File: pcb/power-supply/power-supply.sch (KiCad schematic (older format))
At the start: 2 parts

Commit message: starting pcb design and added teensy pinout table
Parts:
- added J1, J2: Conn_01x20_Female, symbol Conn_01x20_Female
- D1: footprint LEDs:LED_0805 -> (none)
- R1: value R -> 150; footprint Resistors_SMD:R_0805 -> (none)
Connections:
- net labels added: +5V, 5V, B0, B1, B2, B3, B4, B5, B6, B7, C0, C1, C2, C3, C4, C5, C6, D0, D1, D2, D3, D4, D5, D6, D7, E0, E1, E6, E7, F0, F1, F2, F3, F4, F5, F6, F7, VREF, c7
- net labels removed: VCC
- wire segments 3 -> 43
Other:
- note added: "current: 10 mA\nforward voltage: 2.1 V (green)"

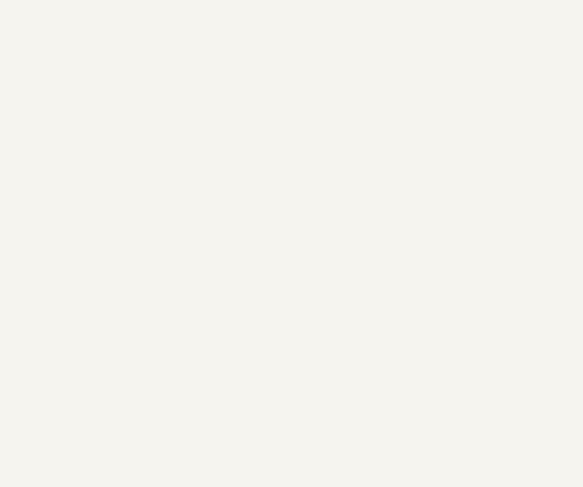
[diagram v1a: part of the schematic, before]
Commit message: added an overcurrent protection circuit to the ltspice simulation and starting the pcb design with the adc pins
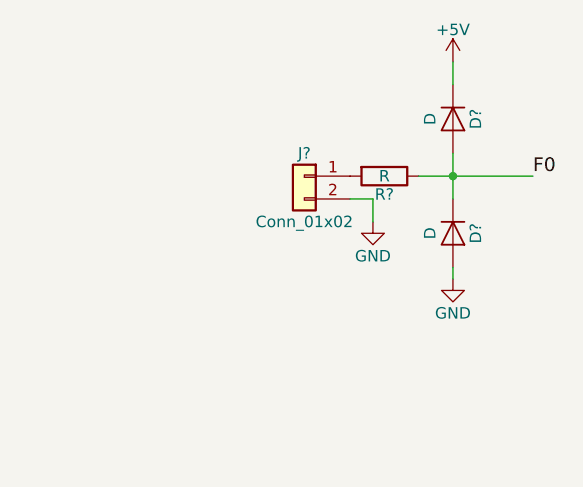
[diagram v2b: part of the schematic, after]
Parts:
- added D? (x2): D, symbol D
- added J?: Conn_01x02, symbol Conn_01x02
- added R?: R, symbol R
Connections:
- net +5V: now also D?.1 (K)
- net F0: now also D?.1 (K), D?.2 (A), R?.1
- net GND: now also D?.2 (A), J?.2 (Pin_2)
- new net: J?.1 (Pin_1), R?.2
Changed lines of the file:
@@
 $Descr A4 11693 8268
 encoding utf-8
-Sheet 1 2
+Sheet 1 1
 Title "Power Supply"
 Date ""
@@
 Text Notes 4000 1550 0    60   ~ 0
 current: 10 mA\nforward voltage: 2.1 V (green)
+$Comp
+L D D?
+U 1 1 5B05C2AC
+P 8500 1000
+F 0 "D?" H 8500 1100 50  0000 C CNN
+F 1 "D" H 8500 900 50  0000 C CNN
+F 2 "" H 8500 1000 50  0001 C CNN
+F 3 "" H 8500 1000 50  0001 C CNN
+	1    8500 1000
+	0    1    1    0
+$EndComp
+$Comp
+L D D?
+U 1 1 5B05C312
+P 8500 1500
+F 0 "D?" H 8500 1600 50  0000 C CNN
+F 1 "D" H 8500 1400 50  0000 C CNN
+F 2 "" H 8500 1500 50  0001 C CNN
+F 3 "" H 8500 1500 50  0001 C CNN
+	1    8500 1500
+	0    1    1    0
+$EndComp
+$Comp
+L R R?
+U 1 1 5B05C34C
+P 8200 1250
+F 0 "R?" V 8280 1250 50  0000 C CNN
+F 1 "R" V 8200 1250 50  0000 C CNN
+F 2 "" V 8130 1250 50  0001 C CNN
+F 3 "" H 8200 1250 50  0001 C CNN
+	1    8200 1250
+	0    1    1    0
+$EndComp
+Wire Wire Line
+	8350 1250 8850 1250
+Wire Wire Line
+	8500 1350 8500 1150
+Connection ~ 8500 1250
+$Comp
+L +5V #PWR?
+U 1 1 5B05C556
+P 8500 750
+F 0 "#PWR?" H 8500 600 50  0001 C CNN
+F 1 "+5V" H 8500 890 50  0000 C CNN
+F 2 "" H 8500 750 50  0001 C CNN
+F 3 "" H 8500 750 50  0001 C CNN
+	1    8500 750
+	1    0    0    -1
+$EndComp
+$Comp
+L GND #PWR?
+U 1 1 5B05C579
+P 8500 1700
+F 0 "#PWR?" H 8500 1450 50  0001 C CNN
+F 1 "GND" H 8500 1550 50  0000 C CNN
+F 2 "" H 8500 1700 50  0001 C CNN
+F 3 "" H 8500 1700 50  0001 C CNN
+	1    8500 1700
+	1    0    0    -1
+$EndComp
+Wire Wire Line
+	8500 750  8500 850
+Wire Wire Line
+	8500 1650 8500 1700
+$Comp
+L Conn_01x02 J?
+U 1 1 5B05C693
+P 7850 1250
+F 0 "J?" H 7850 1350 50  0000 C CNN
+F 1 "Conn_01x02" H 7850 1050 50  0000 C CNN
+F 2 "" H 7850 1250 50  0001 C CNN
+F 3 "" H 7850 1250 50  0001 C CNN
+	1    7850 1250
+	-1   0    0    -1
+$EndComp
+$Comp
+L GND #PWR?
+U 1 1 5B05C783
+P 8150 1450
+F 0 "#PWR?" H 8150 1200 50  0001 C CNN
+F 1 "GND" H 8150 1300 50  0000 C CNN
+F 2 "" H 8150 1450 50  0001 C CNN
+F 3 "" H 8150 1450 50  0001 C CNN
+	1    8150 1450
+	1    0    0    -1
+$EndComp
+Wire Wire Line
+	8050 1350 8150 1350
+Wire Wire Line
+	8150 1350 8150 1450
+Text Label 8850 1250 0    60   ~ 0
+F0
 $EndSCHEMATC

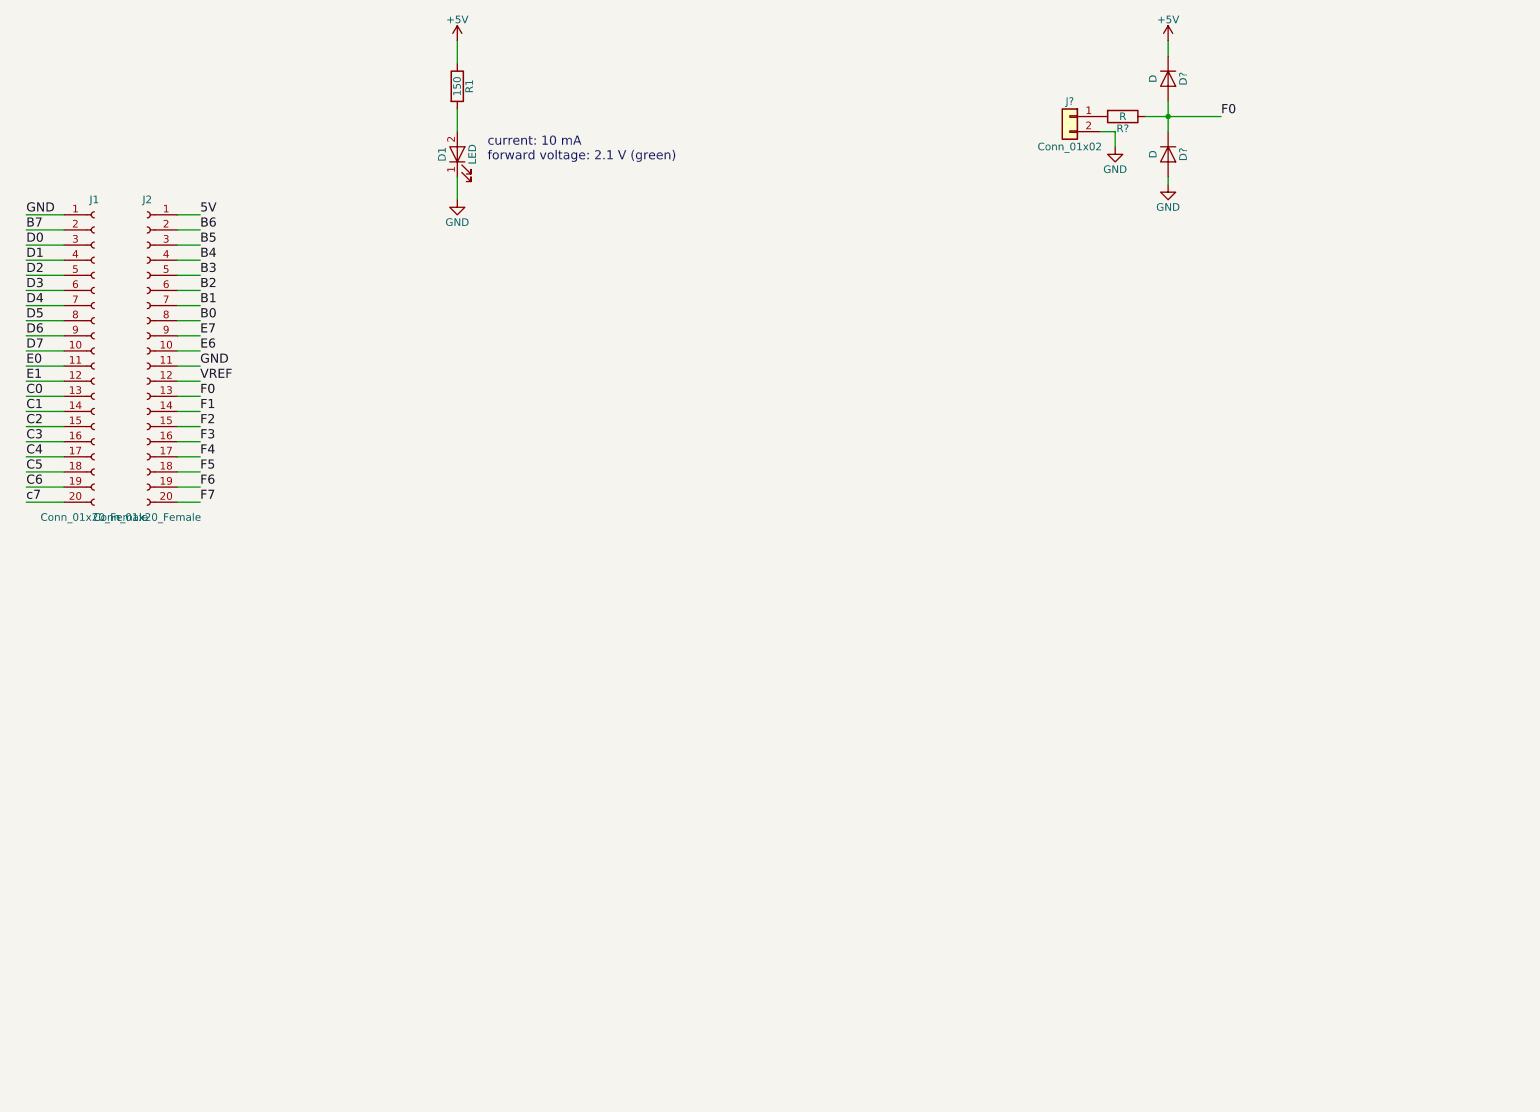
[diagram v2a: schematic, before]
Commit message: starting the pcb circuit design and the layout design. implementing a RJ45 plug, spi pin-header, adc inputs etc
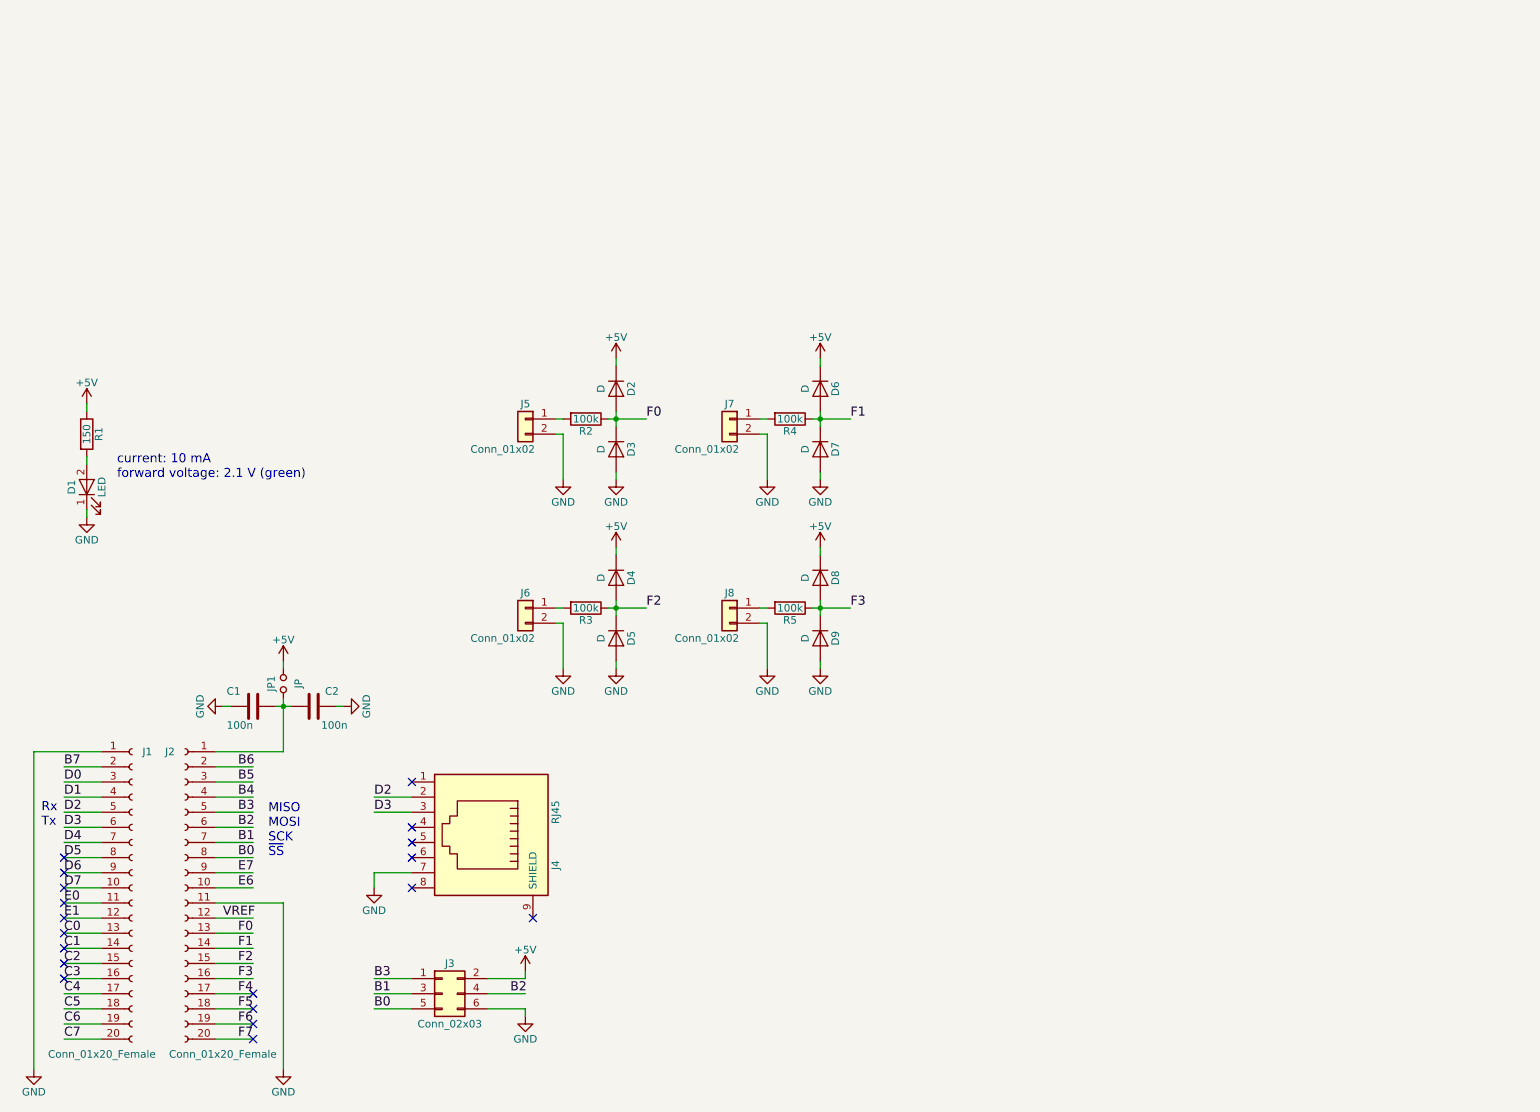
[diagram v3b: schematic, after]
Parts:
- added C1, C2: 100n, Capacitors_SMD:C_0603, symbol C
- added D2, D3, D4, D5, D8, D9: D, Diodes_SMD:D_SOD-523, symbol D
- added J3: Conn_02x03, Pin_Headers:Pin_Header_Straight_2x03_Pitch2.54mm, symbol Conn_02x03_Odd_Even
- added J4: RJ45, Connectors:IQRF_KON-SIM-01, symbol RJ45
- added J5, J6, J8: Conn_01x02, Pin_Headers:Pin_Header_Straight_1x02_Pitch2.54mm, symbol Conn_01x02
- added JP1: JP, Pin_Headers:Pin_Header_Straight_1x02_Pitch2.54mm, symbol Jumper_NO_Small
- added R2, R3, R5: 100k, Resistors_SMD:R_0603, symbol R
- D1: footprint (none) -> LEDs:LED_0603
- D6, D7: renamed from D?; footprint (none) -> Diodes_SMD:D_SOD-523
- J1, J2: footprint (none) -> Socket_Strips:Socket_Strip_Straight_1x20_Pitch2.54mm
- J7: renamed from J?; footprint (none) -> Pin_Headers:Pin_Header_Straight_1x02_Pitch2.54mm
- R1: footprint (none) -> Resistors_SMD:R_0603
- R4: renamed from R?; value R -> 100k; footprint (none) -> Resistors_SMD:R_0603
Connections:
- net labels added: C7
- net labels removed: 5V, c7
- wire segments 49 -> 94
- no-connect marks 0 -> 19
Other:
- note added: "MISO\nMOSI\nSCK\n~SS"
- note added: "Rx\nTx"
- moved on the sheet: D1, D6, D7, J1, J2, J7, R1, R4

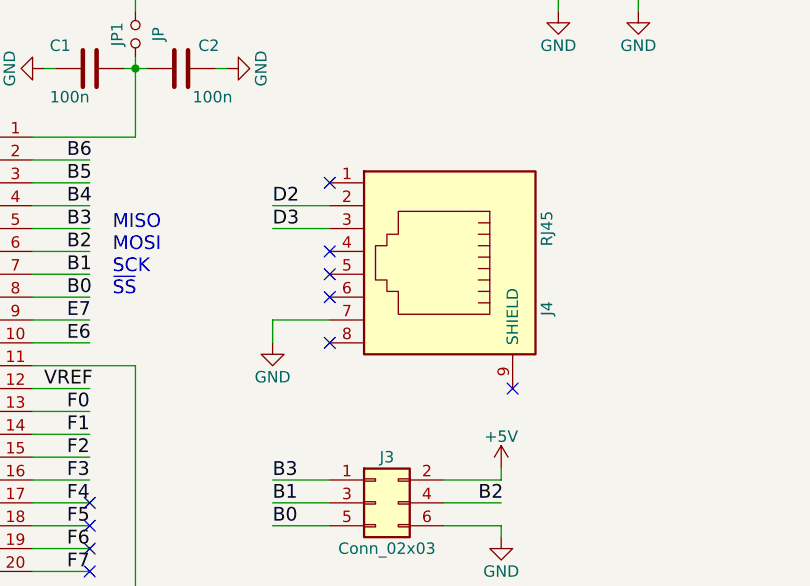
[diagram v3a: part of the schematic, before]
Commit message: removed RJ45 (should have been a RJ11) with a simple 03x01 pinheader for uart
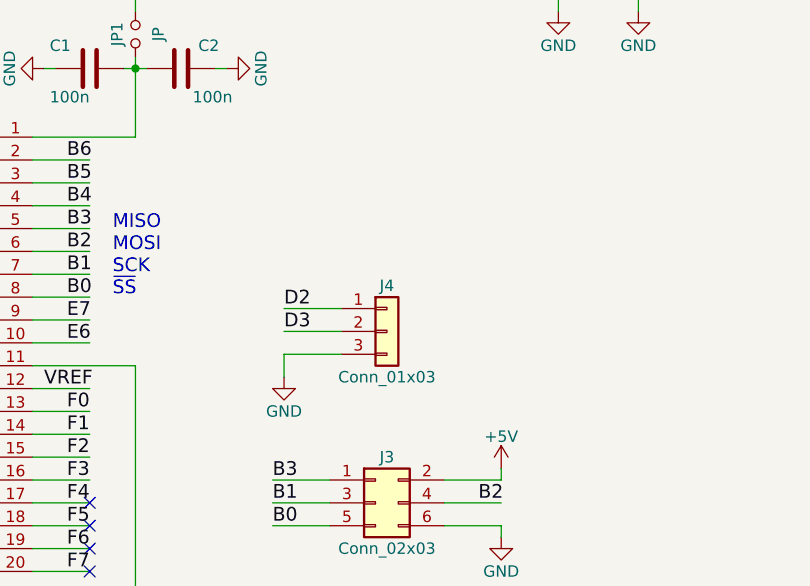
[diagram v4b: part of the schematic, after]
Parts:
- removed J4: RJ45, Connectors:IQRF_KON-SIM-01, symbol RJ45
- added J4: Conn_01x03, Pin_Headers:Pin_Header_Straight_1x03_Pitch2.54mm, symbol Conn_01x03
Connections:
- no-connect marks 19 -> 13
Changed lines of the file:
@@
 Wire Wire Line
 	6200 4100 6200 4150
-$Comp
-L RJ45 J4
-U 1 1 5B075BE1
-P 3950 6000
-F 0 "J4" H 4150 6500 50  0000 C CNN
-F 1 "RJ45" H 3800 6500 50  0000 C CNN
-F 2 "Connectors:IQRF_KON-SIM-01" H 3950 6000 50  0001 C CNN
-F 3 "" H 3950 6000 50  0001 C CNN
-	1    3950 6000
-	0    1    1    0
-$EndComp
 Wire Wire Line
-	3500 5750 3250 5750
-Text Label 3250 5750 0    60   ~ 0
+	3550 6200 3300 6200
+Text Label 3300 6200 0    60   ~ 0
 D2
 Text Notes 1050 5950 0    60   ~ 0
 Rx\nTx
 Wire Wire Line
-	3500 5850 3250 5850
-Text Label 3250 5850 0    60   ~ 0
+	3550 6300 3300 6300
+Text Label 3300 6300 0    60   ~ 0
 D3
 Wire Wire Line
-	3500 6250 3250 6250
+	3550 6400 3300 6400
 Wire Wire Line
-	3250 6250 3250 6350
+	3300 6400 3300 6500
 $Comp
 L GND #PWR020
 U 1 1 5B076183
-P 3250 6350
-F 0 "#PWR020" H 3250 6100 50  0001 C CNN
-F 1 "GND" H 3250 6200 50  0000 C CNN
-F 2 "" H 3250 6350 50  0001 C CNN
-F 3 "" H 3250 6350 50  0001 C CNN
-	1    3250 6350
+P 3300 6500
+F 0 "#PWR020" H 3300 6250 50  0001 C CNN
+F 1 "GND" H 3300 6350 50  0000 C CNN
+F 2 "" H 3300 6500 50  0001 C CNN
+F 3 "" H 3300 6500 50  0001 C CNN
+	1    3300 6500
 	1    0    0    -1
 $EndComp
-NoConn ~ 3500 5650
-NoConn ~ 3500 5950
-NoConn ~ 3500 6050
-NoConn ~ 3500 6150
-NoConn ~ 3500 6350
-NoConn ~ 4300 6550
 $Comp
 L Conn_02x03_Odd_Even J3
@@
 Wire Wire Line
 	4250 7150 4250 7200
+$Comp
+L Conn_01x03 J4
+U 1 1 5B078EF8
+P 3750 6300
+F 0 "J4" H 3750 6500 50  0000 C CNN
+F 1 "Conn_01x03" H 3750 6100 50  0000 C CNN
+F 2 "Pin_Headers:Pin_Header_Straight_1x03_Pitch2.54mm" H 3750 6300 50  0001 C CNN
+F 3 "" H 3750 6300 50  0001 C CNN
+	1    3750 6300
+	1    0    0    -1
+$EndComp
 $EndSCHEMATC
